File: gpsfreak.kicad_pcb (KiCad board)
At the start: 4 copper layers, 79.8 x 47.2 mm, 158 parts, among them J10 Skedd, J13 Boot, J2 SMA, J3 SMA, J4 SMA, J5 U.Fl, J6 SMA, J7 USB_C_Receptacle_16P, J8 U.Fl, J9 U.Fl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

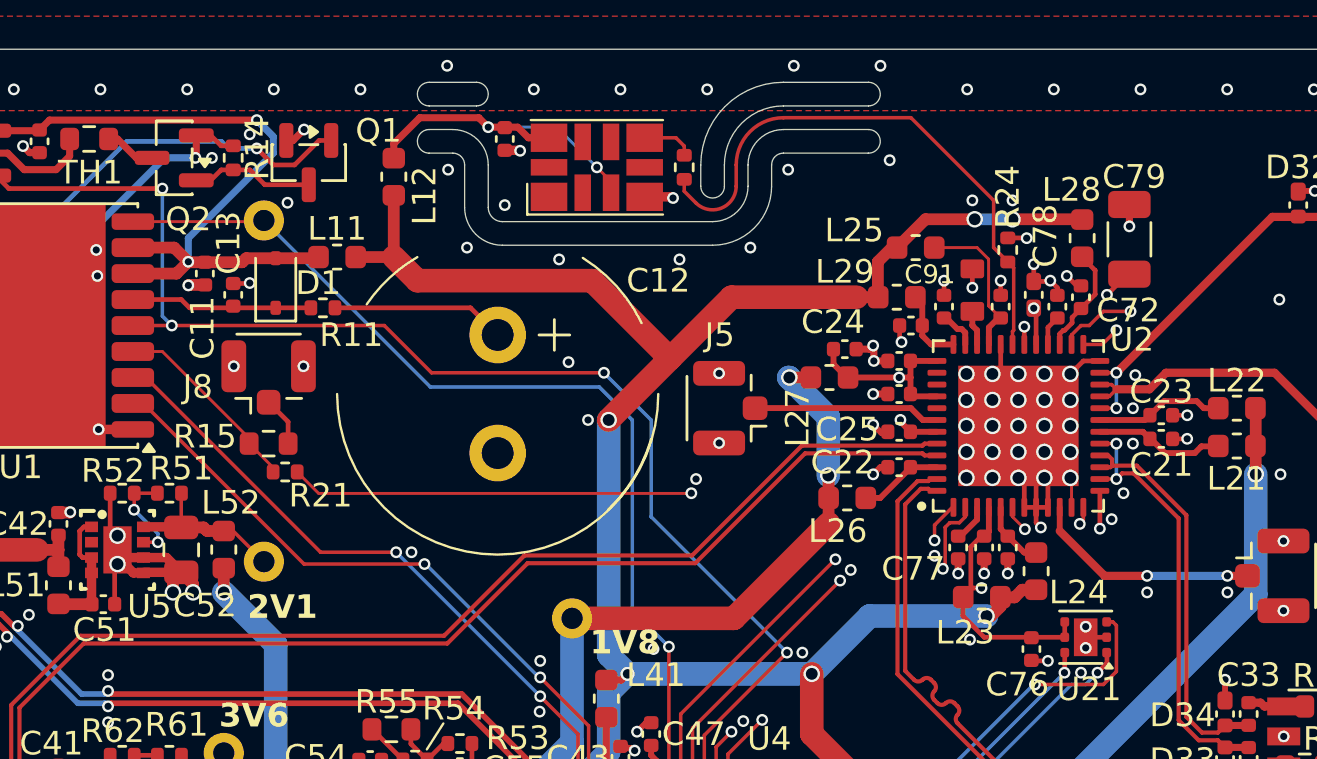
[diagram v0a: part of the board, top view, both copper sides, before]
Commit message: Enlarge the exposed pad under the LMK chip to 11×7 mm.
Also change the DNP flags to avoid the balun by default.
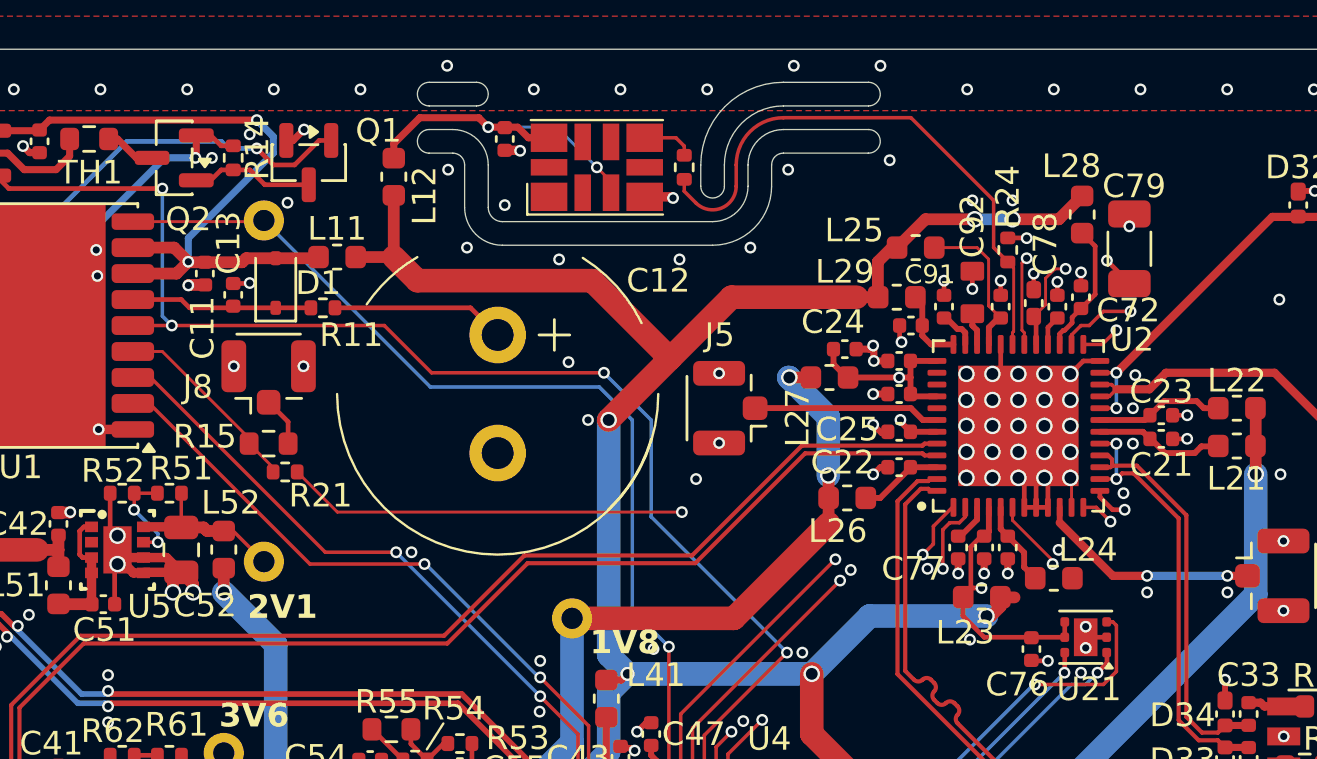
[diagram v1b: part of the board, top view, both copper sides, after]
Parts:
- moved L28 1.00 mm to (158.2, 83.4)
- moved L24 0.81 mm to (157.1, 98.8), turned to 180 degrees
- moved C79 0.40 mm to (160.2, 84.8)
- moved C78 0.35 mm to (156.2, 87.2)
- moved C92 0.10 mm to (153.6, 86.7)
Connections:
- net /Clocking/VDDO_PLL2 renamed /Clocking/VDD_PLL2
- net /Clocking/VDDO_XO renamed /Clocking/VDD_XO
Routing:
- net FINC: track 36.1 -> 40.9 mm
- net /Clocking/GPSCLKLO: track 33.0 -> 36.7 mm
- net /Clocking/VDD_DIG: track 17.0 -> 19.2 mm
- net GND: track 209.2 -> 207.0 mm, vias 299 -> 298
- net PDN: track 22.1 -> 23.8 mm
- net /Clocking/LF1: track 6.01 -> 7.33 mm
- net /Clocking/VDD_PLL1: track 4.61 -> 5.60 mm
- net /Clocking/VDD_IN: track 2.83 -> 3.61 mm
- net +3V3: track 171.7 -> 171.1 mm

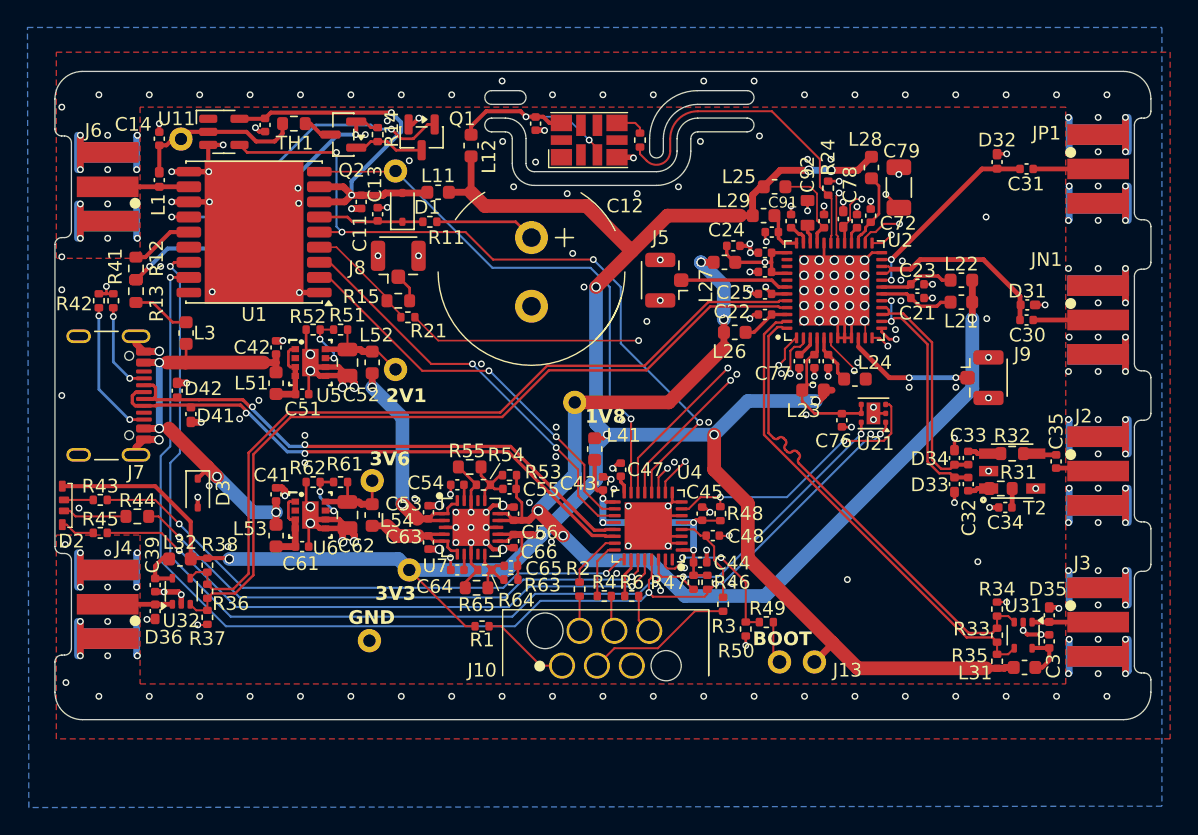
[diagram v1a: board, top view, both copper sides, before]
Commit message: Make all the LED resistors 0603 & adjust values.
Move the LED inwards so it doesn't overhang.
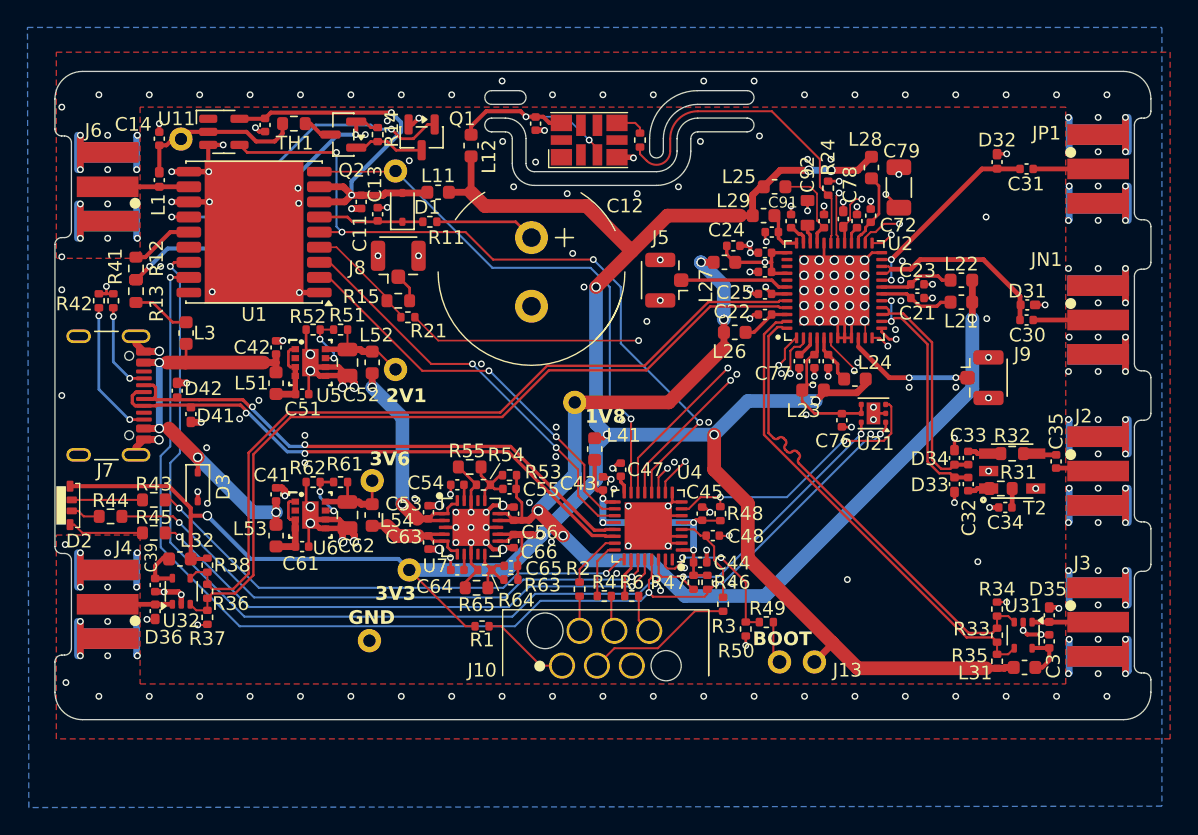
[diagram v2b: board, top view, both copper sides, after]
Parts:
- R43: value 1k -> 330; footprint Resistor_SMD:R_0402_1005Metric -> Resistor_SMD:R_0603_1608Metric
- R45: footprint Resistor_SMD:R_0402_1005Metric -> Resistor_SMD:R_0603_1608Metric
- moved R43 3.90 mm to (106.0, 107.6)
- moved R45 3.90 mm to (106.0, 110.0)
- moved R44 1.95 mm to (102.8, 108.8)
- moved D2 0.56 mm to (99.9, 108.0)
- moved D3 0.45 mm to (109.2, 106.7)
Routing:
- net +3V3: track 171.1 -> 176.2 mm
- net /CPU/Blue: track 41.1 -> 36.9 mm
- net /CPU/Red: track 43.4 -> 39.2 mm
- net Net-(D2-RK): track 2.50 -> 5.52 mm
- net Net-(D2-BK): track 2.13 -> 5.15 mm
- net Net-(D2-GK): track 4.68 -> 2.17 mm
- net /CPU/Green: track 39.7 -> 41.6 mm
- net I2C_SCL: track 106.9 -> 106.3 mm
- net I2C_SDA: track 103.1 -> 102.5 mm

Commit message: Remove the strap resistor on the GPS timepulse U.Fl connector.
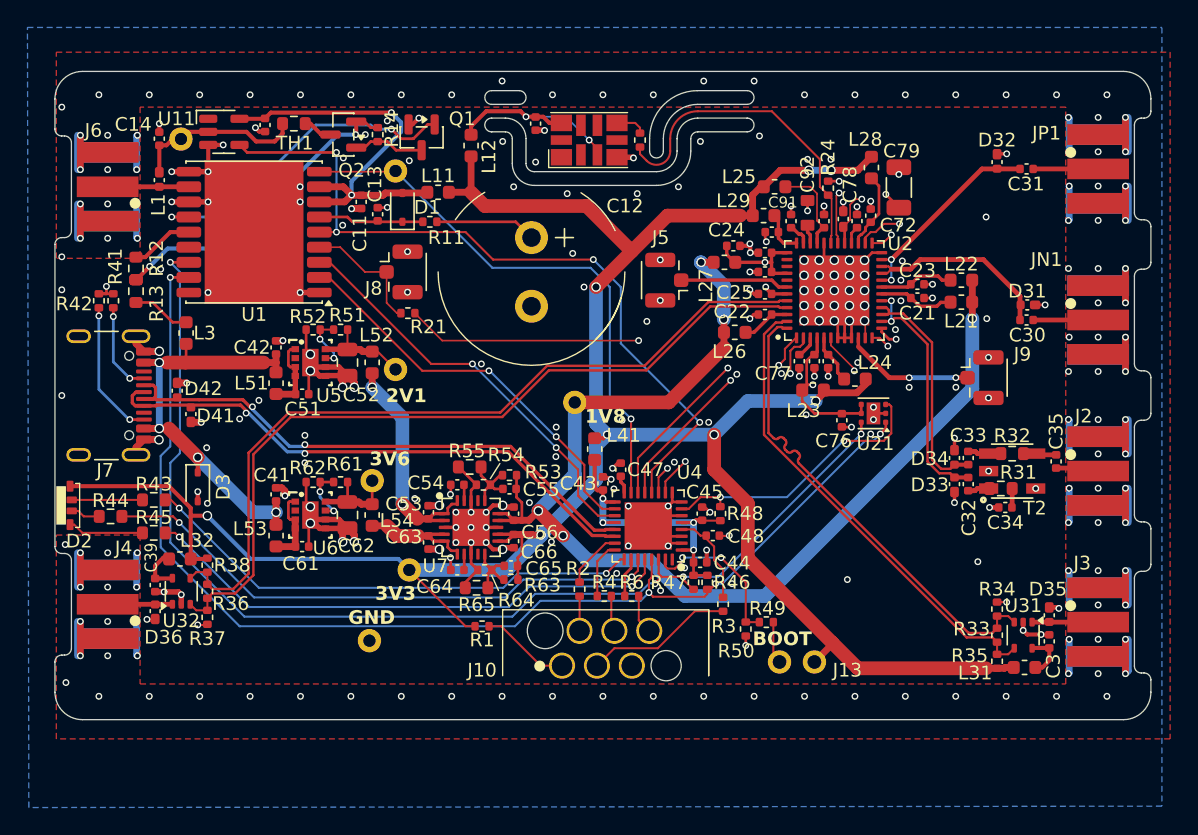
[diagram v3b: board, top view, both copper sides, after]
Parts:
- removed R15: 0, Resistor_SMD:R_0603_1608Metric
- moved J8 0.73 mm to (124.0, 91.0), turned to 0 degrees
- moved R21 0.30 mm to (124.5, 94.0)
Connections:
- J8 pad 1: Net-(J8-In) -> GPSCLK
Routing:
- net Net-(J8-In): track 2.09 -> 0.00 mm
- net GPSCLK: track 8.31 -> 9.25 mm
- net GND: vias 298 -> 300

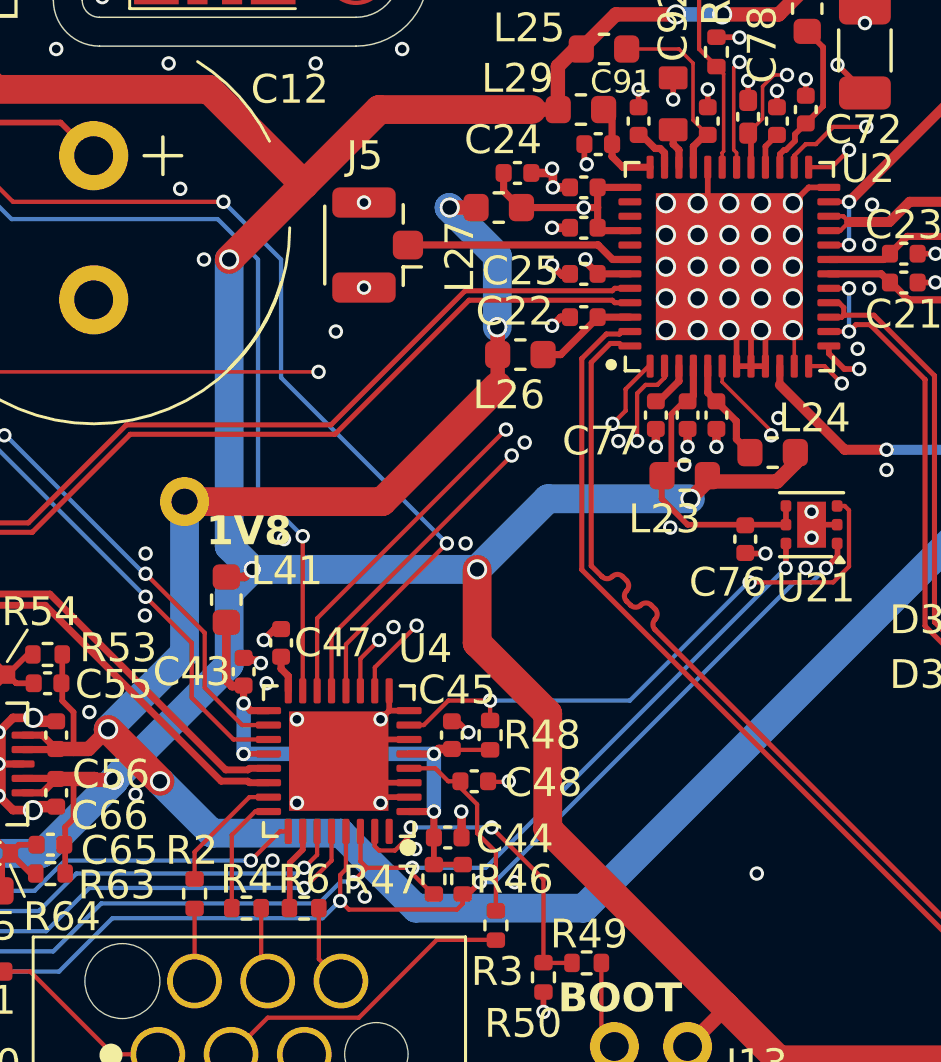
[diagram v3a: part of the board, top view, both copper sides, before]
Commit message: Tiny layout tweaks.
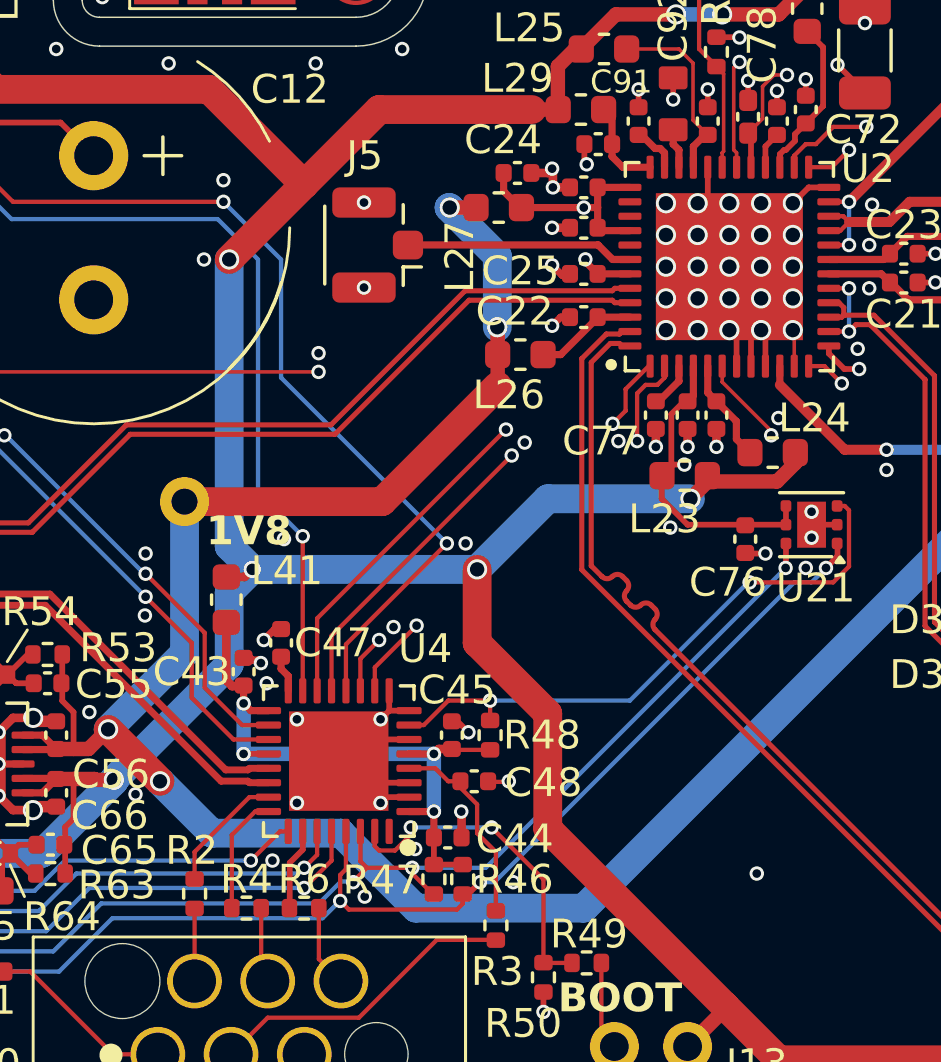
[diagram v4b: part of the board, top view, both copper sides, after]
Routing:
- net GND: track 206.9 -> 205.9 mm
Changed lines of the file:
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@@
-	)
-	(segment
-		(start 155.8 95.8)
-		(end 156.8 95.8)
-		(width 0.2)
-		(layer "F.Cu")
-		(net 1)
 	)
 	(segment
@@
 	)
 	(via
-		(at 148.1 113.7)
+		(at 148.05 113.7)
 		(size 0.5)
 		(drill 0.3)
@@
 	)
 	(via
-		(at 141.9 94.6)
+		(at 141.3 95.35)
 		(size 0.5)
 		(drill 0.3)
@@
 	)
 	(via
-		(at 136.5 89.65)
-		(size 0.5)
-		(drill 0.3)
+		(at 138 89.35)
+		(size 0.5)
+		(drill 0.3)

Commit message: Minor tidy ups and fix a stupid bug.
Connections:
- net /Power/FbCG18 renamed /Power/Fb1V8
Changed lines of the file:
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@@
 	(net 57 "Net-(L3-Pad2)")
 	(net 58 "OUT3_P")
-	(net 59 "/Power/FbCG18")
+	(net 59 "/Power/Fb1V8")
 	(net 60 "/Power/Fb36")
 	(net 61 "/Power/Fb21")
@@
 			(layers "F.Cu" "F.Mask" "F.Paste")
 			(roundrect_rratio 0.25)
-			(net 59 "/Power/FbCG18")
+			(net 59 "/Power/Fb1V8")
 			(pintype "passive")
 		)
@@
 			(layers "F.Cu" "F.Mask" "F.Paste")
 			(roundrect_rratio 0.25)
-			(net 59 "/Power/FbCG18")
+			(net 59 "/Power/Fb1V8")
 			(pintype "passive")
 		)
@@
 			(layers "F.Cu" "F.Mask" "F.Paste")
 			(roundrect_rratio 0.25)
-			(net 59 "/Power/FbCG18")
+			(net 59 "/Power/Fb1V8")
 			(pinfunction "FB1")
 			(pintype "input")
@@
 			(layers "F.Cu" "F.Mask" "F.Paste")
 			(roundrect_rratio 0.25)
-			(net 59 "/Power/FbCG18")
+			(net 59 "/Power/Fb1V8")
 			(pintype "passive")
 		)
@@
 			(layers "F.Cu" "F.Mask" "F.Paste")
 			(roundrect_rratio 0.25)
-			(net 59 "/Power/FbCG18")
+			(net 59 "/Power/Fb1V8")
 			(pintype "passive")
 		)

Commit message: Add LCSC part numbers for a few items.
Don't 'exclude from BOM' things we want to assemble.
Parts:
- TH1: value 220mA -> 220mA or 10Ω

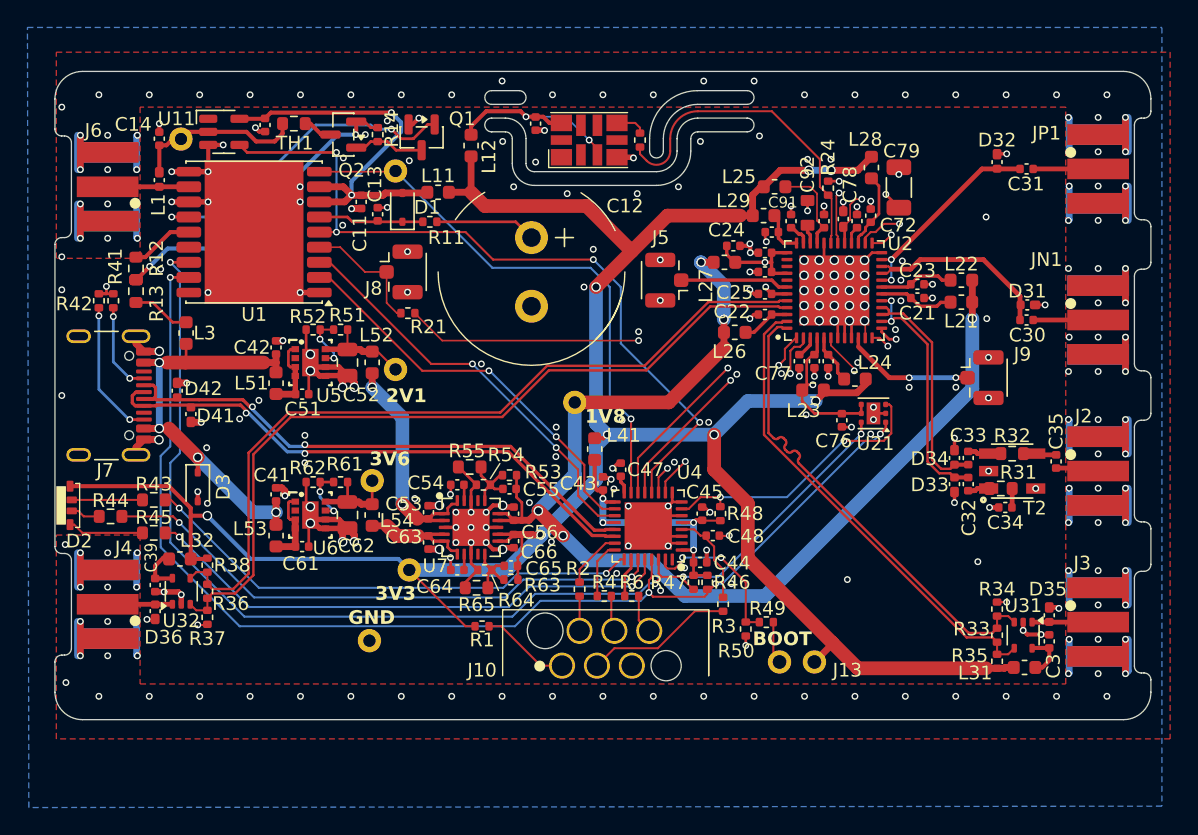
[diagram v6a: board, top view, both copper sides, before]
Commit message: Update all the PCB footprints to match latest kicad.
Use our own SC-70, the latest kicad footprint has oversized pads.
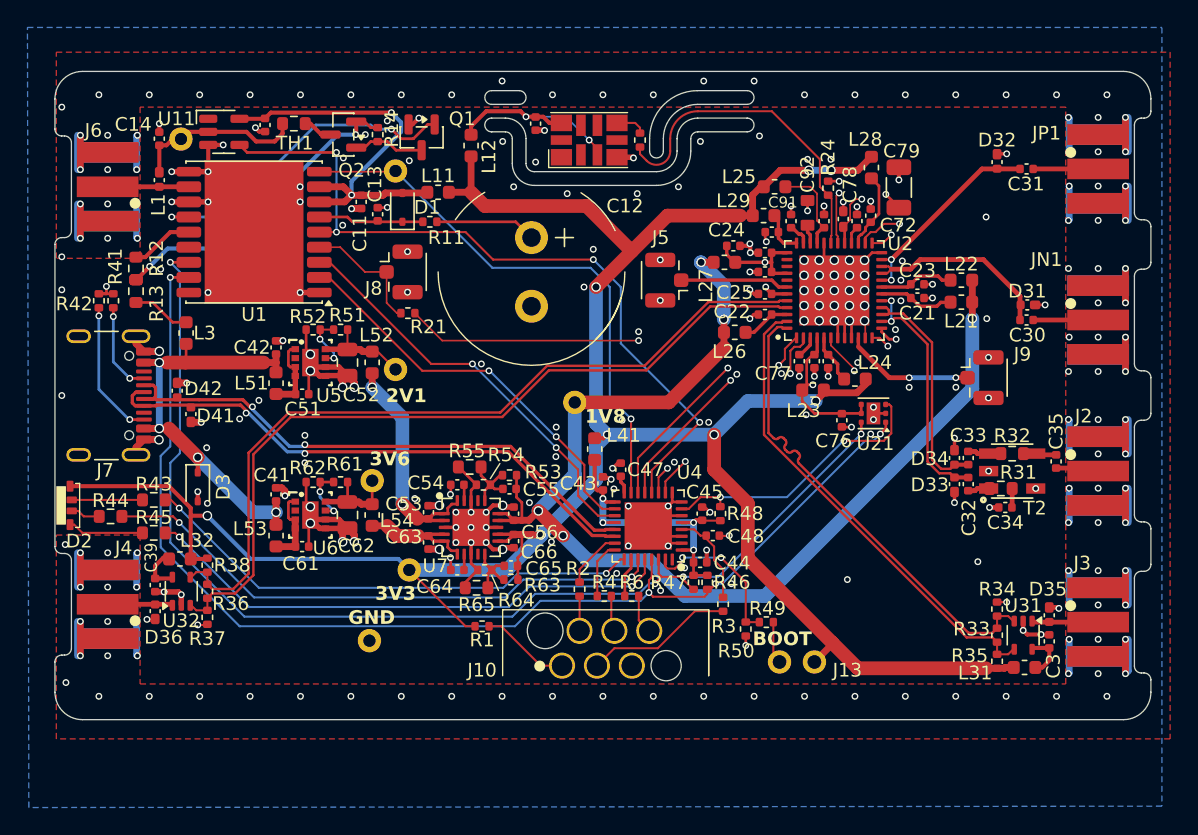
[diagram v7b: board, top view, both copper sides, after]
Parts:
- U31, U32: footprint Package_TO_SOT_SMD:SOT-353_SC-70-5 -> Parts:SOT-353_SC-70-5
